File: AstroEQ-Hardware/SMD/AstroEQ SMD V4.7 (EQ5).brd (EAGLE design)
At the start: 85 x 49 mm, 53 parts, among them IC1 ATMEGA162-16AU, IC2 PIC18F14K50-I/SS, IC3 78L05, J1 POWER_JACKPANEL, M1 Motor Driver, M2 Motor Driver, Q1 NTR4501NT1G, X1 16MHz, X2 12MHz

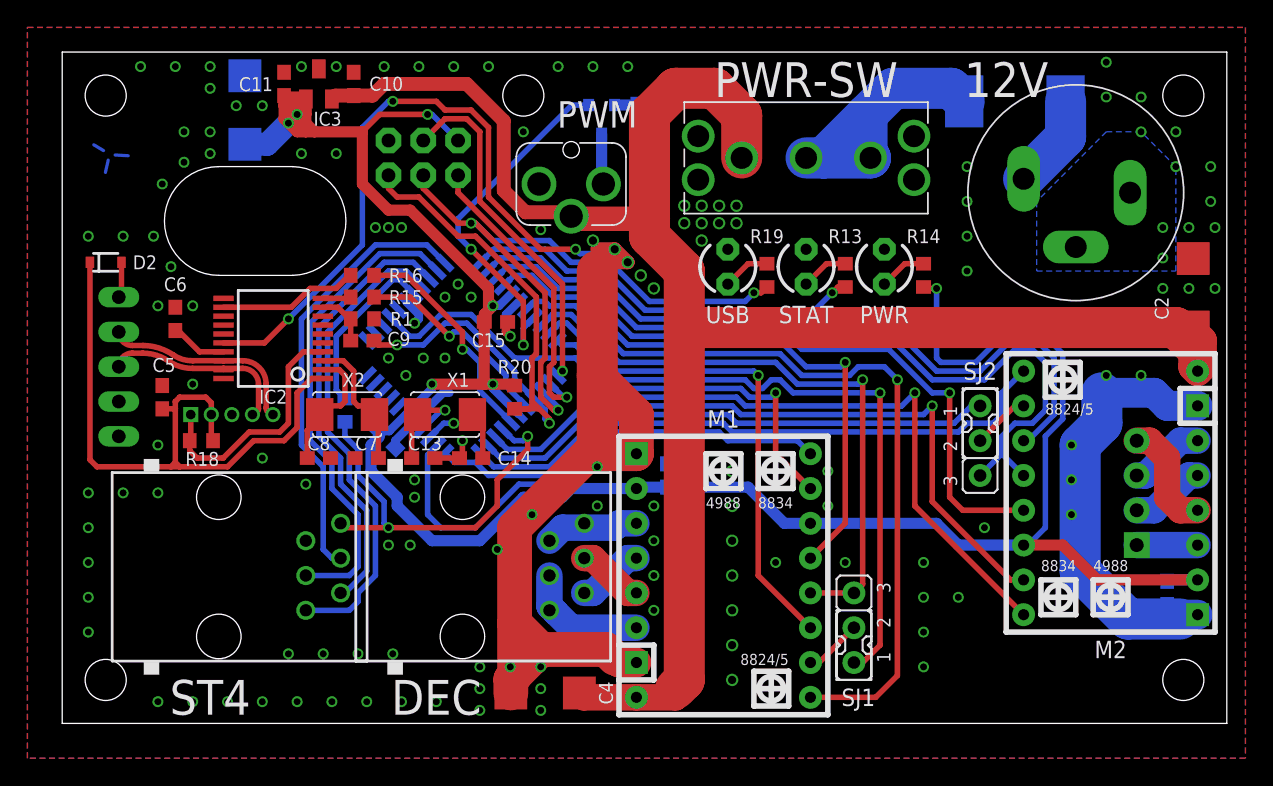
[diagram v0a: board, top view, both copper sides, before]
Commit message: Update AstroEQ PTH/SMD Schematics
1. Tidy up the schematics, add a frame, and improve labelling of nets
2. Add extra textual documentation to the PCB to label the various extra IO pins.
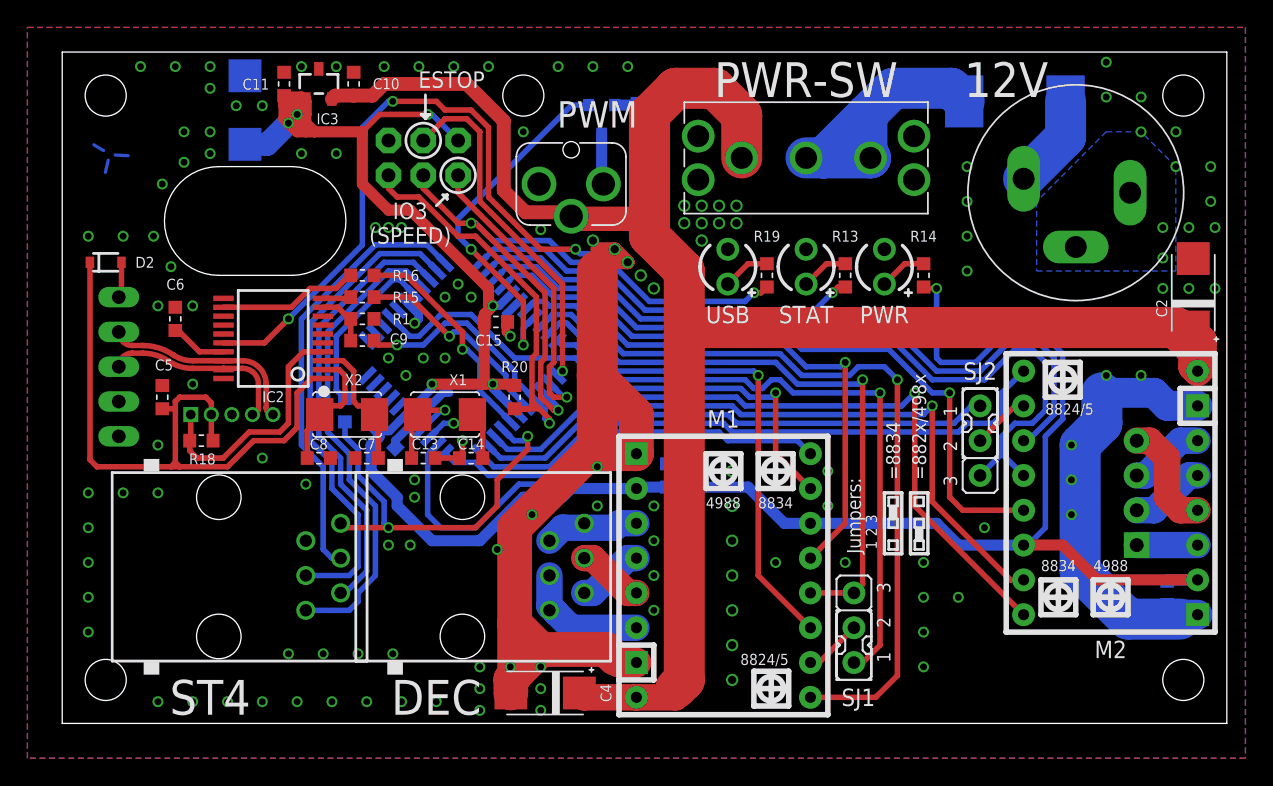
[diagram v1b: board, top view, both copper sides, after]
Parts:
- R15, R16: device SmartPrj:R0603 -> rcl:R0603
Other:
- board text added: "1 2 3"
- board text added: "=882x/498x"
- board text added: "=8834"
- board text added: "ESTOP"
- board text added: "IO3 (SPEED)"
- board text added: "Jumpers:"
- board text added: "V4.7-SMD"
- board text removed: "V4.6-SMD"
